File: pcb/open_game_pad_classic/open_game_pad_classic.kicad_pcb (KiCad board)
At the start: 2 copper layers, 140 x 71 mm, 54 parts, among them J1 COM-09032, J2 COM-09032

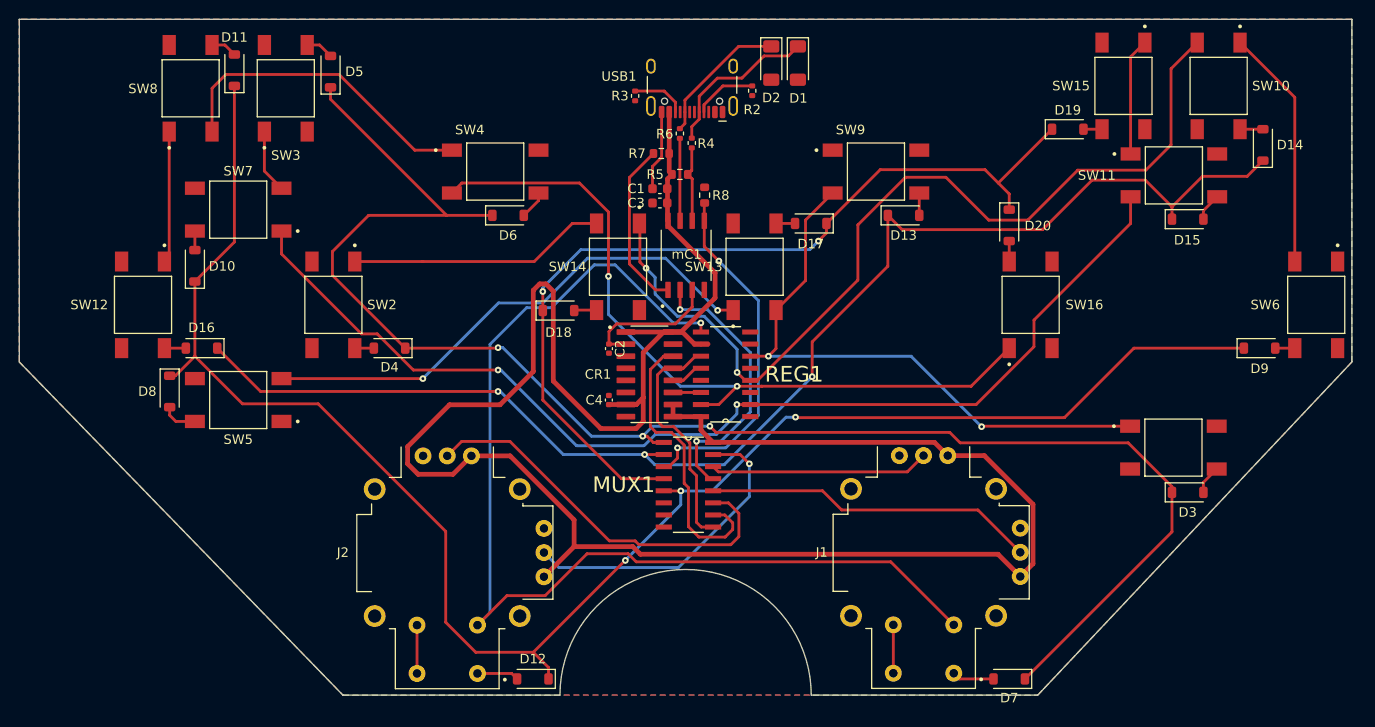
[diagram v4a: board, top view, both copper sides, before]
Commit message: Deleted uneccessary files.
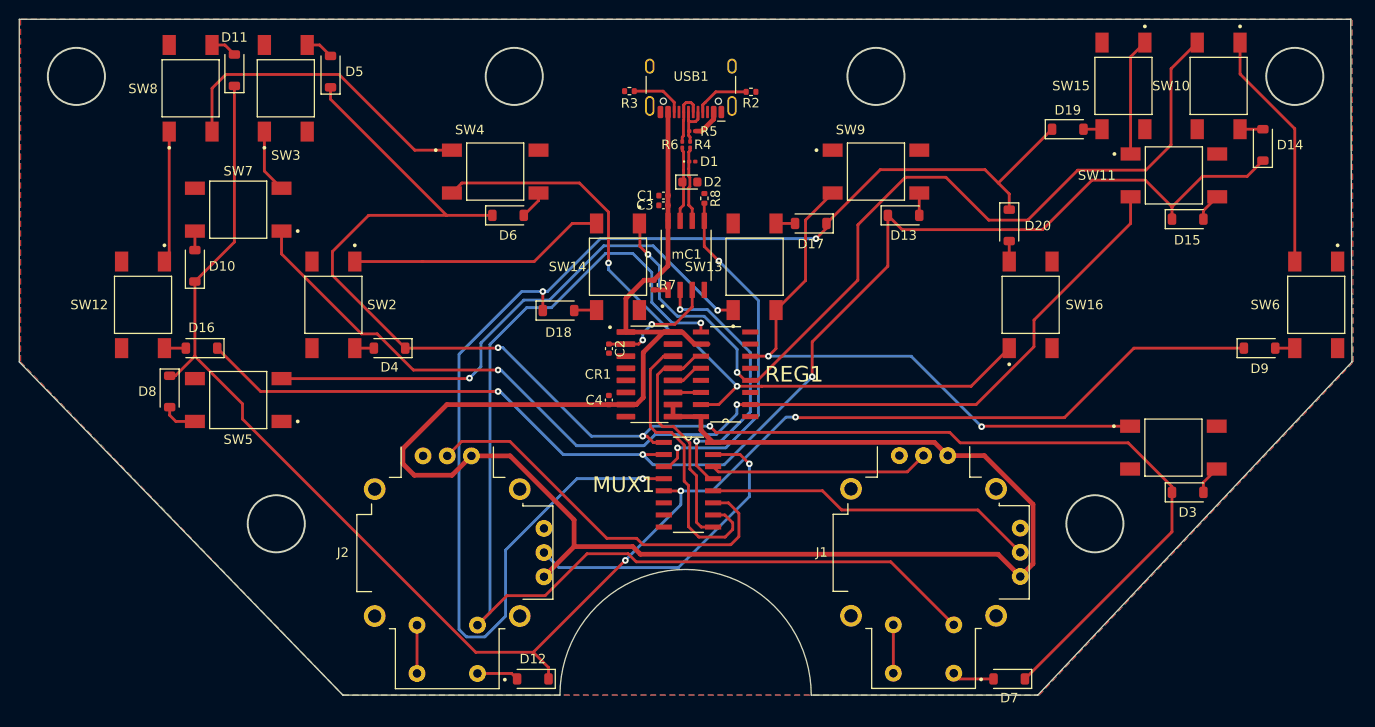
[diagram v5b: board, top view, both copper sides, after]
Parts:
- C1, C3: footprint Capacitor_SMD:C_0603_1608Metric -> Capacitor_SMD:C_0402_1005Metric
- D1: footprint Diode_SMD:D_MiniMELF -> Diode_SMD:D_0201_0603Metric
- D2: footprint Diode_SMD:D_MiniMELF -> Diode_SMD:D_0603_1608Metric
- R4, R6: footprint Resistor_SMD:R_0402_1005Metric -> Resistor_SMD:R_0201_0603Metric
- R5: footprint Resistor_SMD:R_0603_1608Metric -> Resistor_SMD:R_0201_0603Metric
- R7, R8: footprint Resistor_SMD:R_0603_1608Metric -> Resistor_SMD:R_0402_1005Metric
- moved D1 15.2 mm to (145.7, 69.0), turned to 0 degrees
- moved D2 15.1 mm to (145.4, 71.1), turned to 0 degrees
- moved R7 13.8 mm to (141.7, 81.9), turned to 90 degrees
- moved R5 4.73 mm to (145.7, 65.8), turned to 0 degrees
- moved R6 1.20 mm to (144.7, 67.2)
- moved C1 0.82 mm to (142.7, 72.5)
- moved R3 0.78 mm to (139.1, 61.5), turned to 0 degrees
- moved C3 0.45 mm to (142.7, 73.5)
- moved R8 0.34 mm to (147.0, 72.8)
- moved R4 0.25 mm to (145.5, 67.2)
- moved R2 0.17 mm to (151.9, 61.6), turned to 180 degrees
- moved USB1 0.12 mm to (145.6, 60.0)
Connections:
- D1 pad 1: Net-(D1-K) -> /D-
- D2 pad 1: Net-(D2-K) -> /D+
- R4 pad 1: Net-(mC1-PB1) -> /D-
- R4 pad 2: Net-(D1-K) -> /D-
- R5 pad 1: Net-(mC1-PB1) -> /D-
- R6 pad 1: Net-(mC1-PB2) -> /D+
- R6 pad 2: Net-(D2-K) -> /D+
- USB1 pad A6: Net-(D2-K) -> /D+
- USB1 pad A7: Net-(D1-K) -> /D-
- USB1 pad B6: Net-(D2-K) -> /D+
- USB1 pad B7: Net-(D1-K) -> /D-
- mC1 pad 6: Net-(mC1-PB1) -> /D-
- mC1 pad 7: Net-(mC1-PB2) -> /D+
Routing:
- net /X4: track 93.4 -> 140.5 mm, vias 2 -> 3
- net +5V: track 230.0 -> 203.2 mm
- net Net-(D1-K): track 17.3 -> 0.00 mm
- net Net-(mC1-~{RESET}/PB5): track 17.8 -> 1.50 mm
- net Net-(D2-K): track 14.6 -> 0.00 mm
- net /D+: track 0.00 -> 13.8 mm
- net /D-: track 0.00 -> 13.1 mm
- net Net-(mC1-PB2): track 8.71 -> 0.00 mm
- net GND: track 8.45 -> 0.00 mm
- net Net-(mC1-PB1): track 8.01 -> 0.00 mm
- net /X2: track 181.7 -> 177.0 mm
- net /Y5: track 115.4 -> 118.2 mm
- net /Y1: track 127.9 -> 125.1 mm
- net /Y4: track 117.9 -> 120.4 mm
- net /CLK: track 14.7 -> 12.6 mm, vias 0 -> 2
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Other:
- outline, holes or cut-outs redrawn
- board text added: "${REFERENCE}"
